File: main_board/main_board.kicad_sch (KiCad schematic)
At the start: 0 parts

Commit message: initial connection of ISA, IDE and RAM
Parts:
- added J1: Bus_ISA_8bit, symbol Connector:Bus_ISA_8bit
- added J2: IDE_44pin, symbol Connector_Retro:IDE_44pin
- added J3: SIMM_30pin, symbol Connector_Retro:SIMM_30pin
- added U1: M6117D, Package_QFP:PQFP-208_28x28mm_P0.5mm, symbol ALi:M6117D
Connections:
- new net +5V: J1.29 (VCC), J1.3 (VCC), J2.41 (+5VL), J2.42 (+5VM), J3.1 (VCC), J3.30 (VCC), U1.1 (VCC), U1.105 (VCC), U1.125 (VCC), U1.137 (VCC), U1.15 (VCC), U1.150 (VCC), U1.157 (VCC), U1.182 (VCC), U1.197 (~{MASTER}), U1.38 (VCC), U1.46 (VCC), U1.53 (VCC), U1.59 (VCC), U1.76 (VCC), U1.85 (VCC)
- new net AEN: J1.42 (AEN), U1.199 (AEN)
- new net ALE: J1.28 (ALE), U1.173 (BALE)
- new net CAS0: J3.2 (~{CAS}), U1.93 (~{CAS0L})
- new net DA0: J1.19 (~{DACK0}), U1.16 (~{DACK0})
- new net DA1: J1.17 (~{DACK1}), U1.18 (~{DACK1})
- new net DA2: J1.26 (~{DACK2}), U1.20 (~{DACK2})
- new net DA3: J1.15 (~{DACK3}), U1.22 (~{DACK3})
- new net DRQ1: J1.18 (DRQ1), U1.19 (DRQ1)
- new net DRQ2: J1.6 (DRQ2), U1.21 (DRQ2)
- new net DRQ3: J1.16 (DRQ3), U1.23 (DRQ3)
- new net GND: J1.1 (GND), J1.10 (GND), J1.31 (GND), J2.19 (GND), J2.2 (GND), J2.22 (GND), J2.24 (GND), J2.26 (GND), J2.30 (GND), J2.40 (GND), J2.43 (GND), J3.22 (GND), J3.9 (GND), U1.104 (GND), U1.118 (GND), U1.121 (GND), U1.132 (GND), U1.156 (GND), U1.161 (GND), U1.169 (GND), U1.188 (GND), U1.208 (GND), U1.31 (GND), U1.40 (GND), U1.52 (GND), U1.65 (GND), U1.8 (GND), U1.81 (GND), U1.94 (GND)
- new net ICS0: J2.37 (~{CS0}), U1.50 (~{HDCS0})
- new net ICS1: J2.38 (~{CS1}), U1.54 (~{HDCS1})
- new net IOCH: J1.32 (IO), U1.196 (~{IOCHK})
- new net IOR: J1.14 (~{IOR}), J2.25 (~{DIOR}), U1.166 (~{IOR})
- new net IORD: J1.41 (IO_READY), J2.27 (IORDY), U1.164 (IOCHRDY)
- new net IOW: J1.13 (~{IOW}), J2.23 (~{DIOW}), U1.167 (~{IOW})
- new net IRQ3: J1.25 (IRQ3), U1.152 (IRQ3)
- new net IRQ4: J1.24 (IRQ4), U1.151 (IRQ4)
- new net IRQ5: J1.23 (IRQ5), U1.149 (IRQ5)
- new net IRQ6: J1.22 (IRQ6), U1.148 (IRQ6)
- new net IRQ7: J1.21 (IRQ7), U1.147 (IRQ7)
- new net MA0: J3.4 (A0), U1.108 (MA0)
- new net MA1: J3.5 (A1), U1.107 (MA1)
- new net MA10: J3.19 (A10), U1.96 (MA10)
- new net MA11: J3.24 (A11), U1.95 (MA11)
- new net MA2: J3.7 (A2), U1.106 (MA2)
- new net MA3: J3.8 (A3), U1.103 (MA3)
- new net MA4: J3.11 (A4), U1.102 (MA4)
- new net MA5: J3.12 (A5), U1.101 (MA5)
- new net MA6: J3.14 (A6), U1.100 (MA6)
- new net MA7: J3.15 (A7), U1.99 (MA7)
- new net MA8: J3.17 (A8), U1.98 (MA8)
- new net MA9: J3.18 (A9), U1.97 (MA9)
- new net MD0: J3.3 (DQ0), U1.75 (BD0)
- new net MD1: J3.6 (DQ1), U1.74 (BD1)
- new net MD2: J3.10 (DQ2), U1.73 (BD2)
- new net MD3: J3.13 (DQ3), U1.72 (BD3)
- new net MD4: J3.16 (DQ4), U1.71 (BD4)
- new net MD5: J3.20 (DQ5), U1.70 (BD5)
- new net MD6: J3.23 (DQ6), U1.69 (BD6)
- new net MD7: J3.25 (DQ7), U1.68 (BD7)
- new net MWE: J3.21 (~{WE}), U1.79 (~{WE})
- new net RAS0: J3.27 (~{RAS}), U1.84 (~{RAS0})
- new net SA0: J1.62 (BA00), U1.195 (SA0)
- new net SA1: J1.61 (BA01), U1.194 (SA1)
- new net SA10: J1.52 (BA10), U1.184 (SA10)
- new net SA11: J1.51 (BA11), U1.183 (SA11)
- new net SA12: J1.50 (BA12), U1.181 (SA12)
- new net SA13: J1.49 (BA13), U1.180 (SA13)
- new net SA14: J1.48 (BA14), U1.179 (SA14)
- new net SA15: J1.47 (BA15), U1.178 (SA15)
- new net SA16: J1.46 (BA16), U1.177 (SA16)
- new net SA17: J1.45 (BA17), U1.176 (SA17)
- new net SA18: J1.44 (BA18), U1.175 (SA18)
- new net SA19: J1.43 (BA19), U1.174 (SA19)
- new net SA2: J1.60 (BA02), U1.193 (SA2)
- new net SA3: J1.59 (BA03), U1.192 (SA3)
- new net SA4: J1.58 (BA04), U1.191 (SA4)
- new net SA5: J1.57 (BA05), U1.190 (SA5)
- new net SA6: J1.56 (BA06), U1.189 (SA6)
- new net SA7: J1.55 (BA07), U1.187 (SA7)
- new net SA8: J1.54 (BA08), U1.186 (SA8)
- new net SA9: J1.53 (BA09), U1.185 (SA9)
- new net SD0: J1.40 (DB0), J2.17 (DD0), U1.145 (SD0)
- new net SD1: J1.39 (DB1), J2.15 (DD1), U1.144 (SD1)
- new net SD10: J2.8 (DD10), U1.7 (SD10)
- new net SD11: J2.10 (DD11), U1.9 (SD11)
- new net SD12: J2.12 (DD12), U1.10 (SD12)
- new net SD13: J2.14 (DD13), U1.11 (SD13)
- new net SD14: J2.16 (DD14), U1.12 (SD14)
- new net SD15: J2.18 (DD15), U1.13 (SD15)
- new net SD2: J1.38 (DB2), J2.13 (DD2), U1.143 (SD2)
- new net SD3: J1.37 (DB3), J2.11 (DD3), U1.142 (SD3)
- new net SD4: J1.36 (DB4), J2.9 (DD4), U1.141 (SD4)
- new net SD5: J1.35 (DB5), J2.7 (DD5), U1.140 (SD5)
- new net SD6: J1.34 (DB6), J2.5 (DD6), U1.139 (SD6)
- new net SD7: J1.33 (DB7), J2.3 (DD7), U1.138 (SD7)
- new net SD8: J2.4 (DD8), U1.5 (SD8)
- new net SD9: J2.6 (DD9), U1.6 (SD9)
- new net SMR: J1.12 (~{SMEMR}), U1.168 (~{SMEMR})
- new net SMW: J1.11 (~{SMEMW}), U1.170 (~{SMEMW})
- new net TC: J1.27 (TC), U1.14 (TC)
- no-connect marks 0 -> 8

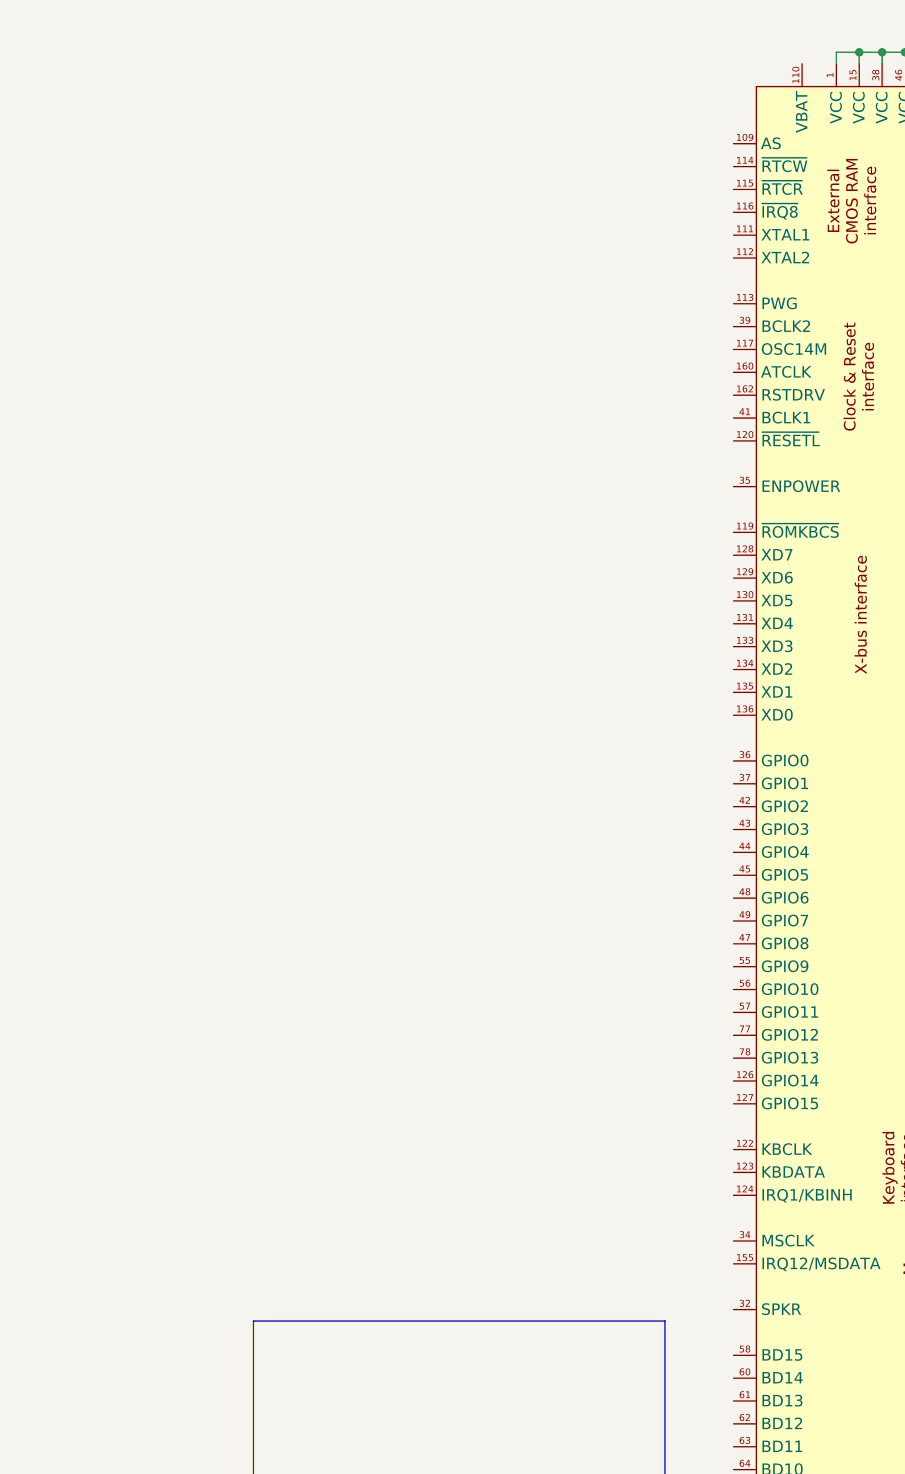
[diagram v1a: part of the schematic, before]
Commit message: add speaker, keyboard, mouse and power connectors
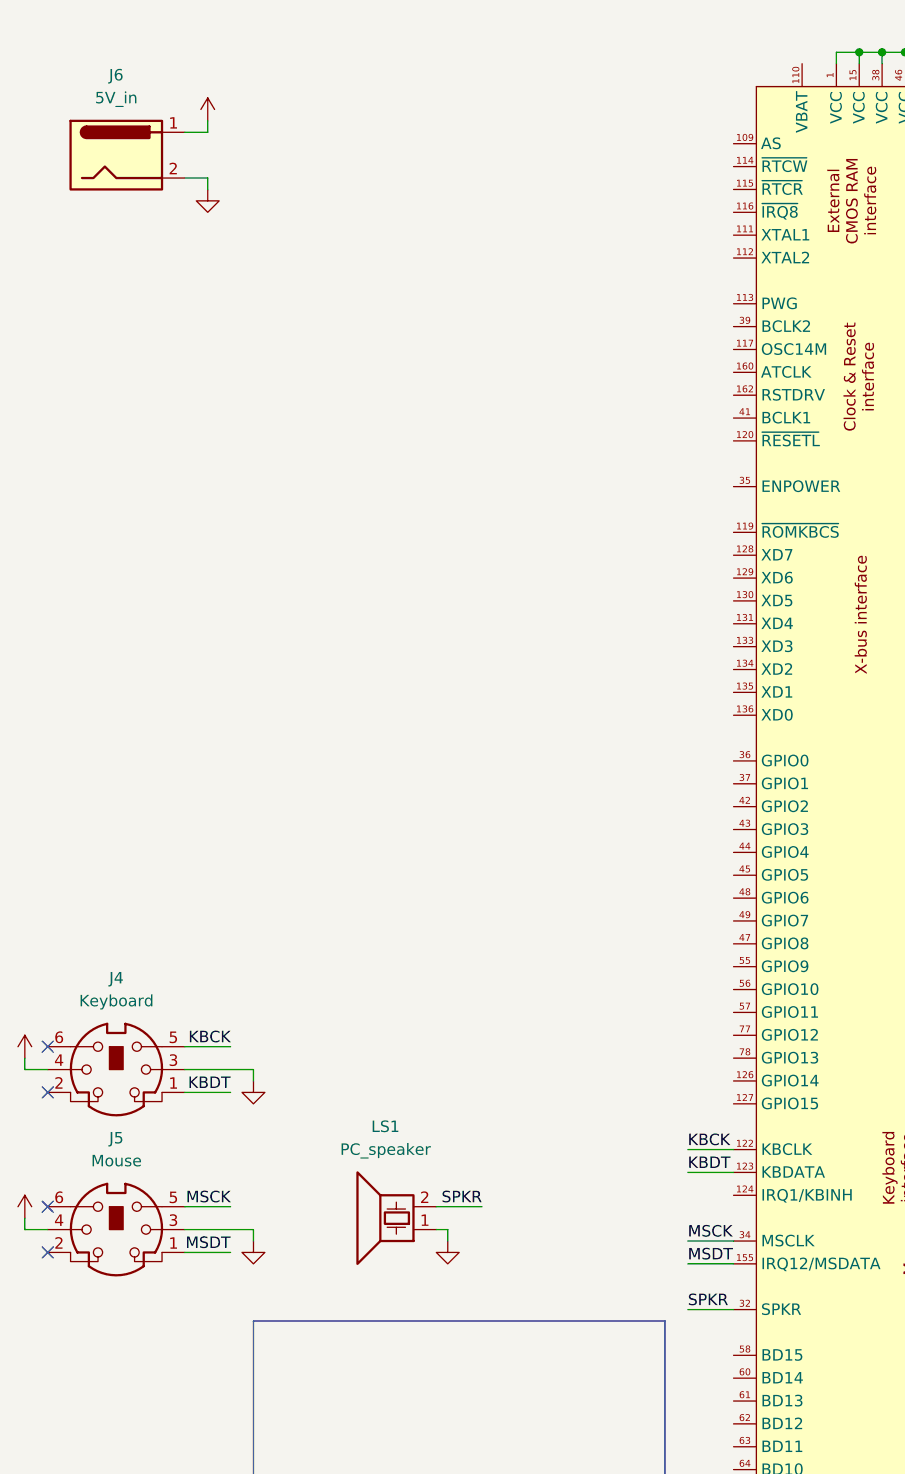
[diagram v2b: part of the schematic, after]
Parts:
- added J4: Keyboard, symbol Connector:Mini-DIN-6
- added J5: Mouse, symbol Connector:Mini-DIN-6
- added J6: 5V_in, symbol Connector:Barrel_Jack
- added LS1: PC_speaker, symbol Device:Speaker_Crystal
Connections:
- net +5V: now also J4.4, J5.4, J6.1
- net GND: now also J4.3, J5.3, J6.2, LS1.1
- net KBCK: now reaches U1.122 (KBCLK)
- net KBCK: now also J4.5
- net KBDT: now reaches U1.123 (KBDATA)
- net KBDT: now also J4.1
- net MSDT: now reaches U1.155 (IRQ12/MSDATA)
- net MSDT: now also J5.1
- net SPKR: now reaches U1.32 (SPKR)
- net SPKR: now also LS1.2
- net MSCK: now reaches U1.34 (MSCLK)
- net MSCK: now also J5.5
- no-connect marks 8 -> 12

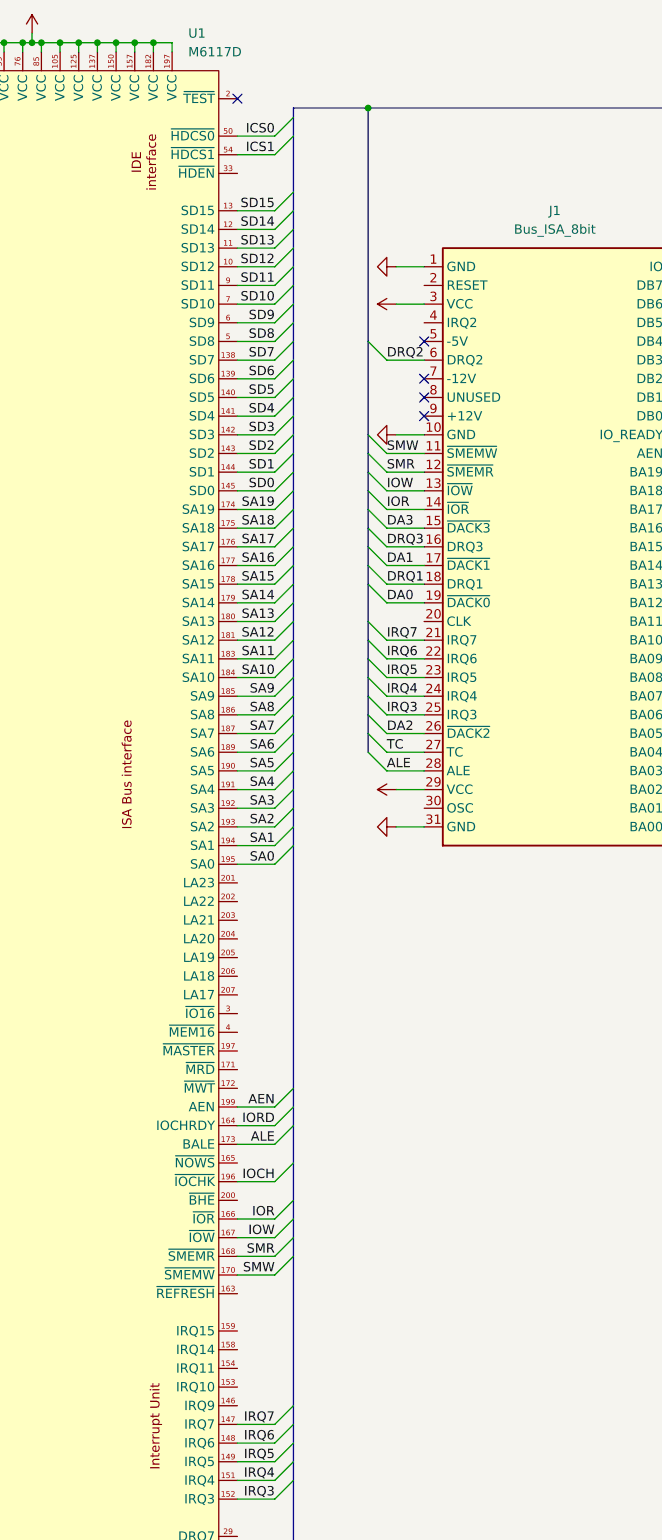
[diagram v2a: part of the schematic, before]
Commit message: connect IRQ9 to ISA bus
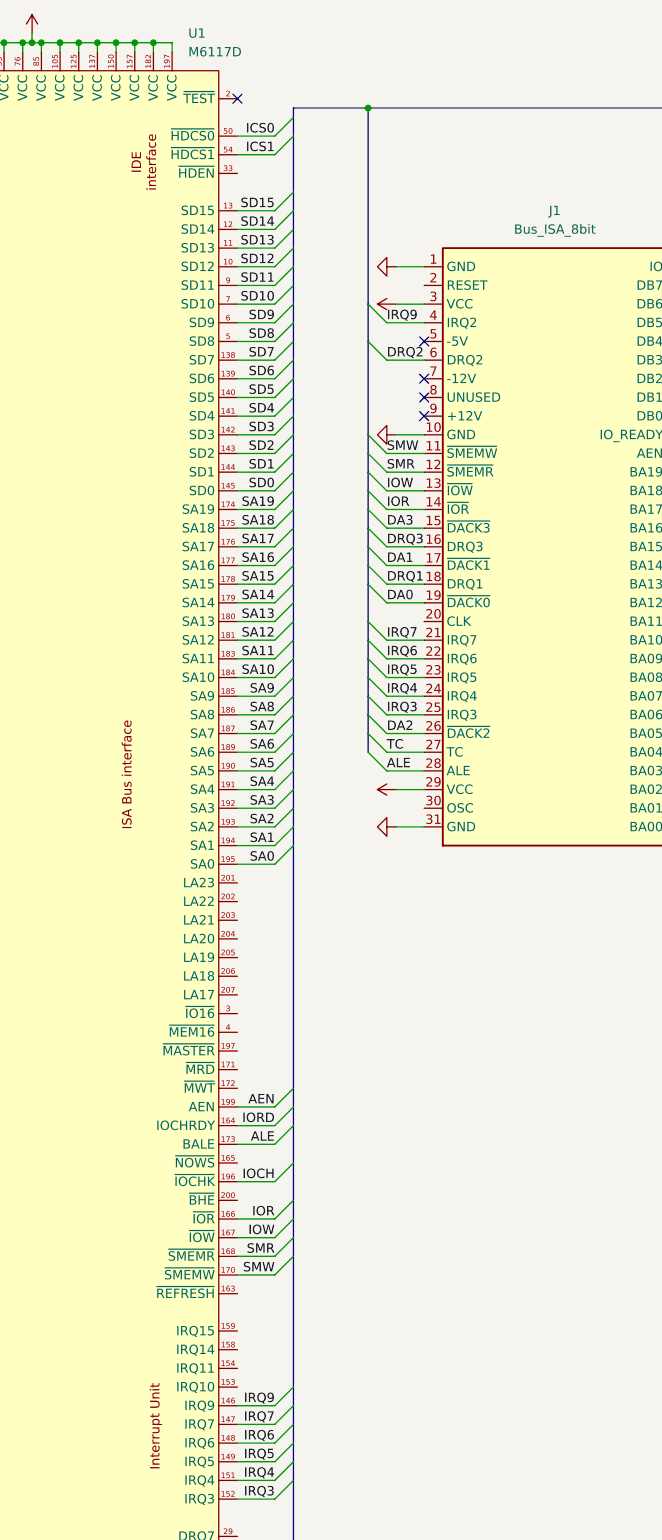
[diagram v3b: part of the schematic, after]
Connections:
- net IRQ9: now reaches J1.4 (IRQ2)
- net IRQ9: now also U1.146 (IRQ9)
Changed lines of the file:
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@@
 	)
 	(bus_entry
+		(at 172.72 199.39)
+		(size -2.54 2.54)
+		(stroke
+			(width 0)
+			(type default)
+		)
+	)
+	(bus_entry
 		(at 53.34 232.41)
 		(size 2.54 -2.54)
@@
 	)
 	(bus_entry
+		(at 182.88 52.07)
+		(size 2.54 2.54)
+		(stroke
+			(width 0)
+			(type default)
+		)
+	)
+	(bus_entry
 		(at 170.18 49.53)
 		(size 2.54 -2.54)
@@
 	(wire
 		(pts
+			(xy 170.18 201.93) (xy 165.1 201.93)
+		)
+		(stroke
+			(width 0)
+			(type default)
+		)
+	)
+	(wire
+		(pts
 			(xy 109.22 242.57) (xy 104.14 242.57)
 		)
@@
 	(bus
 		(pts
-			(xy 172.72 181.61) (xy 172.72 201.93)
+			(xy 172.72 181.61) (xy 172.72 199.39)
 		)
 		(stroke
@@
 		)
 	)
+	(bus
+		(pts
+			(xy 172.72 199.39) (xy 172.72 201.93)
+		)
+		(stroke
+			(width 0)
+			(type default)
+		)
+	)
 	(wire
 		(pts
@@
 		)
 	)
+	(bus
+		(pts
+			(xy 182.88 52.07) (xy 182.88 57.15)
+		)
+		(stroke
+			(width 0)
+			(type default)
+		)
+	)
 	(wire
 		(pts
@@
 	(wire
 		(pts
+			(xy 185.42 54.61) (xy 190.5 54.61)
+		)
+		(stroke
+			(width 0)
+			(type default)
+		)
+	)
+	(wire
+		(pts
 			(xy 226.06 87.63) (xy 231.14 87.63)
 		)
@@
 	(bus
 		(pts
-			(xy 182.88 25.4) (xy 182.88 57.15)
+			(xy 182.88 25.4) (xy 182.88 52.07)
 		)
 		(stroke
@@
 		)
 	)
+	(label "IRQ9"
+		(at 185.42 54.61 0)
+		(fields_autoplaced yes)
+		(effects
+			(font
+				(size 1.27 1.27)
+			)
+			(justify left bottom)
+		)
+	)
 	(label "MD3"
 		(at 53.34 234.95 180)
@@
 		)
 	)
+	(label "IRQ9"
+		(at 170.18 201.93 180)
+		(fields_autoplaced yes)
+		(effects
+			(font
+				(size 1.27 1.27)
+			)
+			(justify right bottom)
+		)
+	)

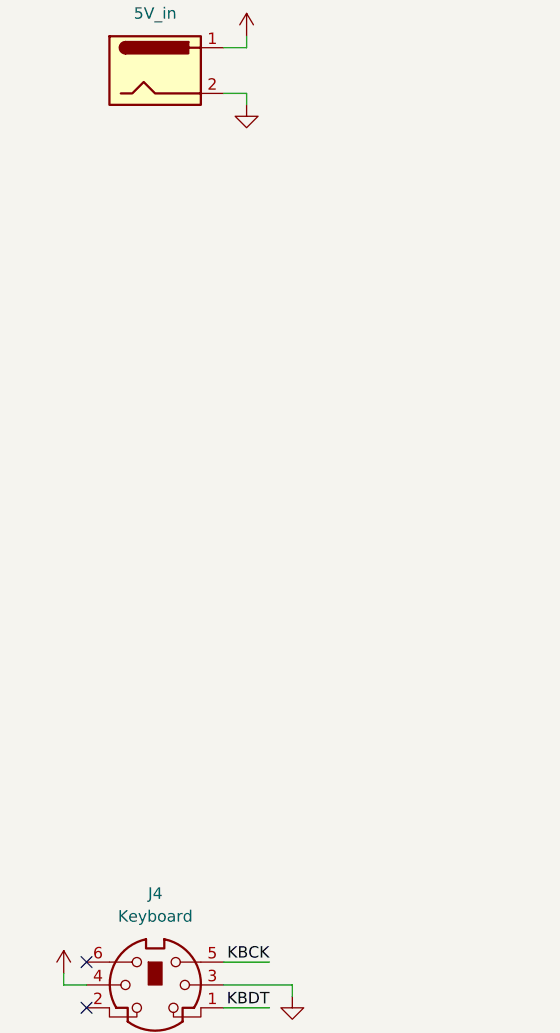
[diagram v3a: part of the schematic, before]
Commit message: add a CMOS flash for BIOS
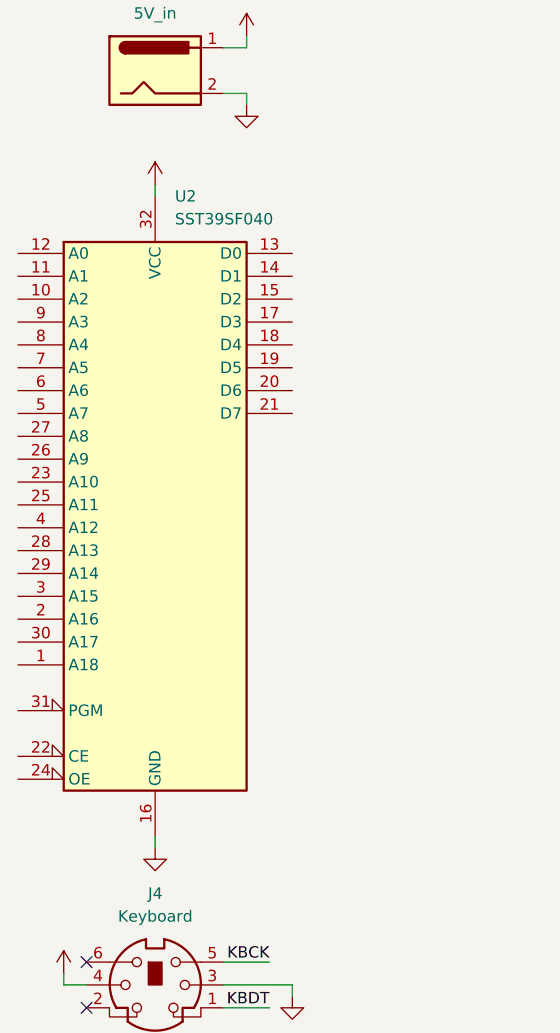
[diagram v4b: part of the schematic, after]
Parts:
- added U2: SST39SF040, symbol Memory_Flash:SST39SF040
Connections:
- net +5V: now also U2.32 (VCC)
- net GND: now also U2.16 (GND)
